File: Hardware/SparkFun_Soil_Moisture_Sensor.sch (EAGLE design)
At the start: 12 parts, among them Q1 2N3904

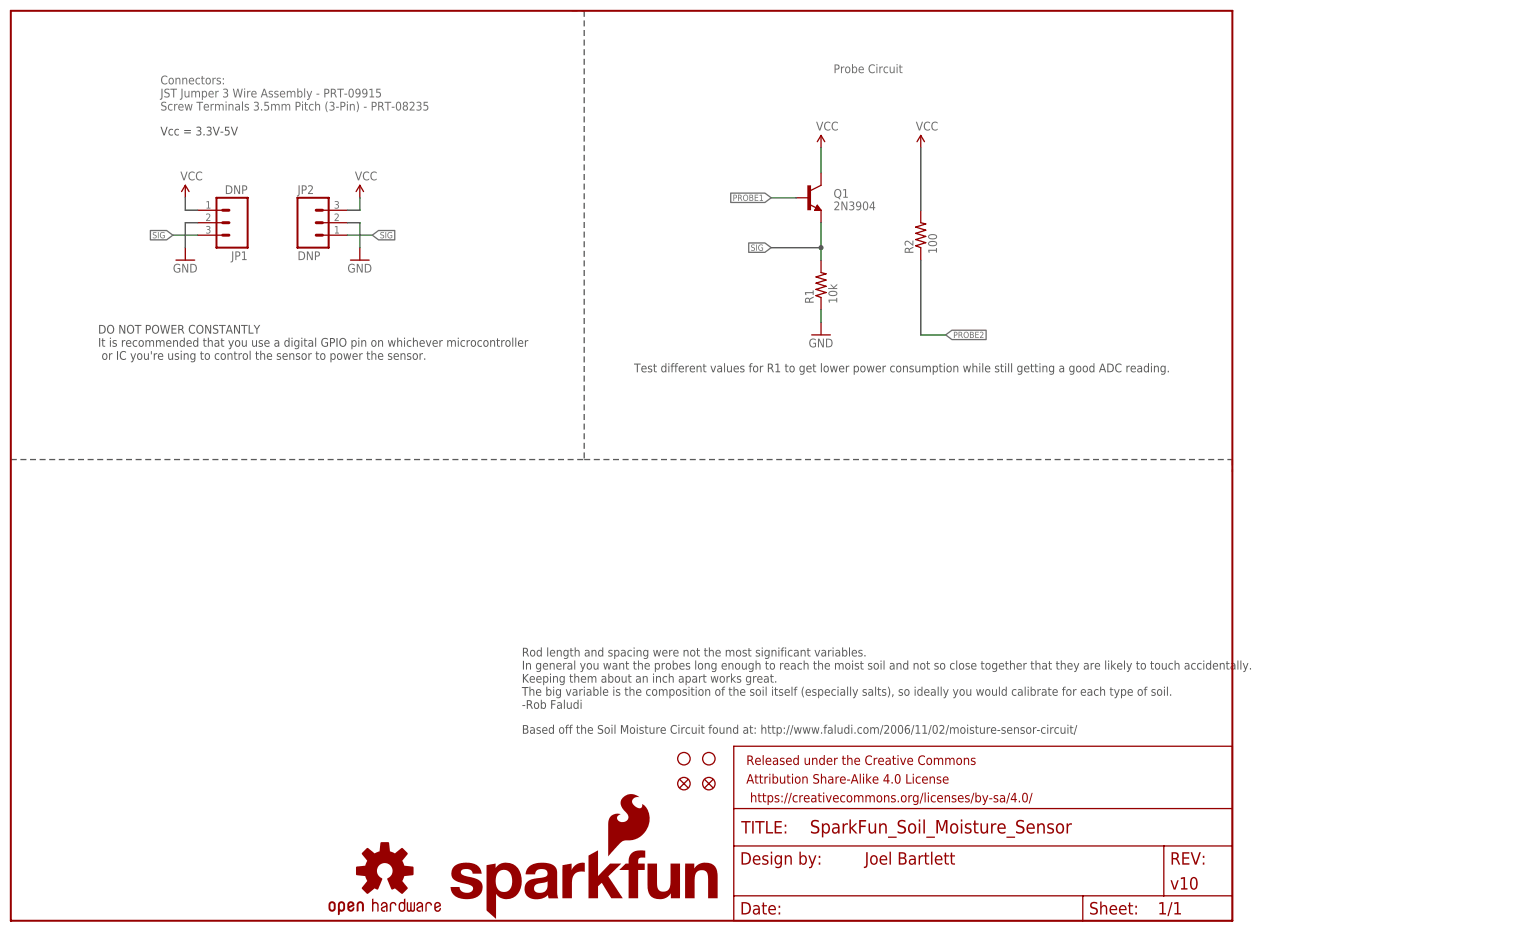
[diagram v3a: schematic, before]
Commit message: Added Locking 3-pin 3.5mm footprint
Added Locking 3-pin 3.5mm footprint for selective soldering.
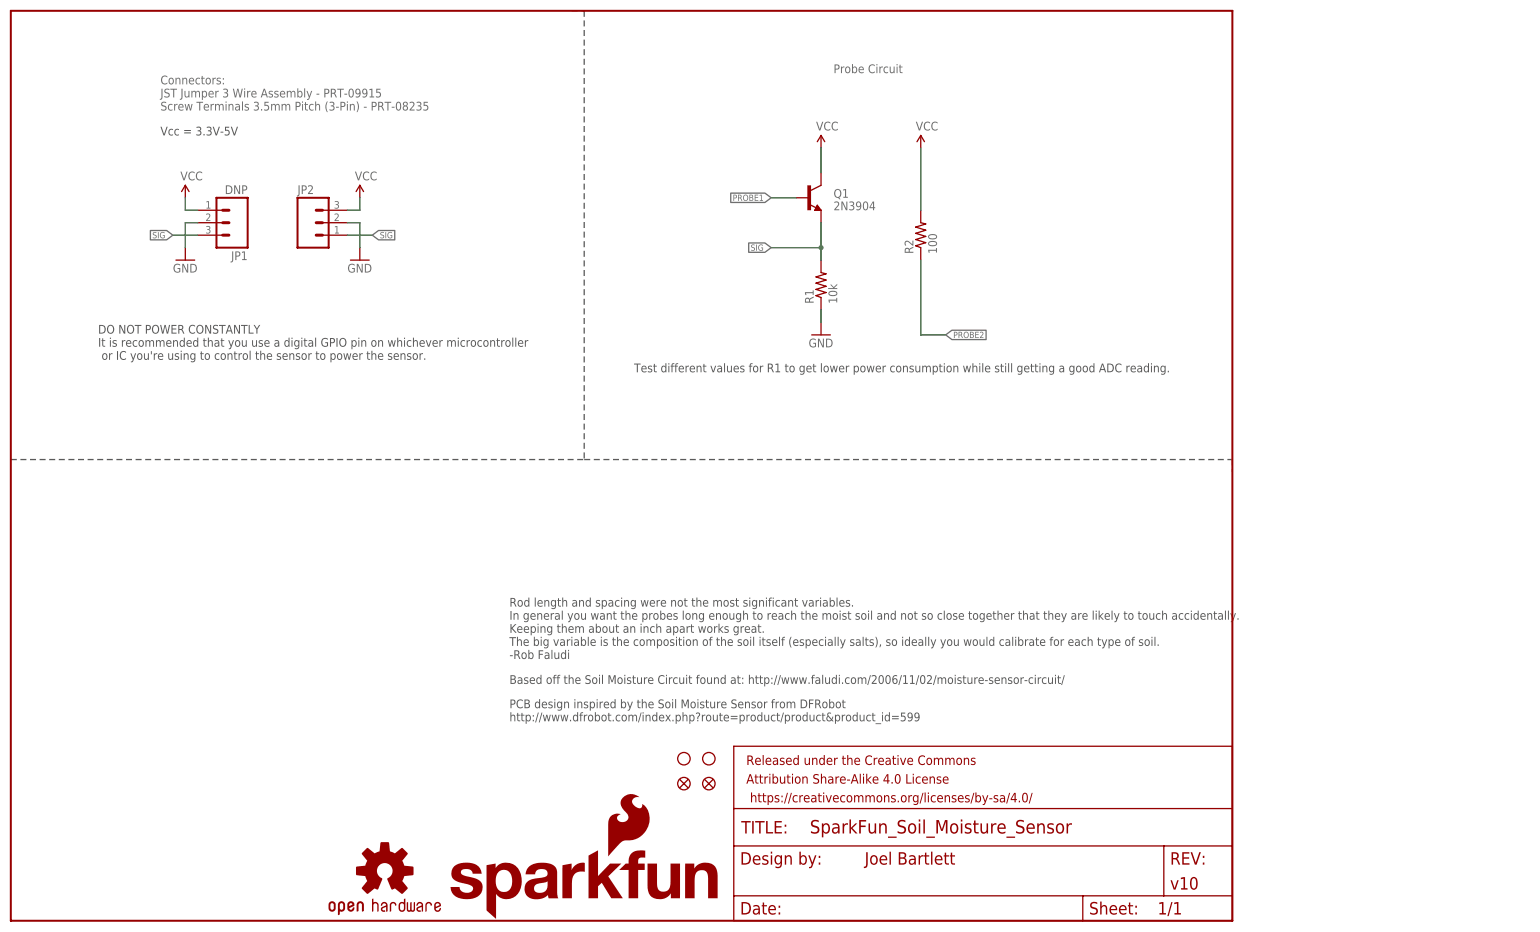
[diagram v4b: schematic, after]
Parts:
- JP2: value DNP -> (none); device SparkFun-Connectors:M03SCREW -> SparkFun-Connectors:M03SCREW_LOCK
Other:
- note added: "PCB design inspired by the Soil Moisture Sensor from DFRobot http://www.dfrobot.com/index.php?route=product/product&product_id=599"
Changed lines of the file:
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@@
 <part name="LOGO2" library="SparkFun-Aesthetics" deviceset="OSHW-LOGO" device="S"/>
 <part name="JP1" library="SparkFun-Connectors" deviceset="M03" device="POLAR" value="DNP"/>
-<part name="JP2" library="SparkFun-Connectors" deviceset="M03" device="SCREW" value="DNP"/>
 <part name="SUPPLY4" library="SparkFun-Aesthetics" deviceset="VCC" device=""/>
 <part name="GND3" library="SparkFun-Aesthetics" deviceset="GND" device=""/>
@@
 <part name="FID1" library="SparkFun-Aesthetics" deviceset="FIDUCIAL" device="1X2"/>
 <part name="FID2" library="SparkFun-Aesthetics" deviceset="FIDUCIAL" device="1X2"/>
+<part name="JP2" library="SparkFun-Connectors" deviceset="M03" device="SCREW_LOCK"/>
 </parts>
 <sheets>
@@
 <wire x1="114.3" y1="185.42" x2="116.84" y2="185.42" width="0.2032" layer="97" style="dashdot"/>
 <wire x1="116.84" y1="185.42" x2="116.84" y2="93.98" width="0.2032" layer="97" style="shortdash"/>
-<text x="104.14" y="38.1" size="1.778" layer="97">Based off the Soil Moisture Circuit found at: http://www.faludi.com/2006/11/02/moisture-sensor-circuit/</text>
-<text x="104.14" y="43.18" size="1.778" layer="97">Rod length and spacing were not the most significant variables.
+<text x="101.6" y="48.26" size="1.778" layer="97">Based off the Soil Moisture Circuit found at: http://www.faludi.com/2006/11/02/moisture-sensor-circuit/</text>
+<text x="101.6" y="53.34" size="1.778" layer="97">Rod length and spacing were not the most significant variables.
 In general you want the probes long enough to reach the moist soil and not so close together that they are likely to touch accidentally.
 Keeping them about an inch apart works great.
@@
 It is recommended that you use a digital GPIO pin on whichever microcontroller
  or IC you're using to control the sensor to power the sensor. </text>
+<text x="101.6" y="40.64" size="1.778" layer="97">PCB design inspired by the Soil Moisture Sensor from DFRobot
+http://www.dfrobot.com/index.php?route=product/product&amp;product_id=599</text>
 </plain>
 <instances>
@@
 <instance part="LOGO2" gate="G$1" x="76.2" y="10.16"/>
 <instance part="JP1" gate="G$1" x="45.72" y="142.24" rot="R180"/>
-<instance part="JP2" gate="G$1" x="60.96" y="142.24"/>
 <instance part="SUPPLY4" gate="G$1" x="35.56" y="147.32"/>
 <instance part="GND3" gate="1" x="35.56" y="134.62"/>
@@
 <instance part="FID1" gate="G$1" x="137.16" y="27.94"/>
 <instance part="FID2" gate="G$1" x="142.24" y="27.94"/>
+<instance part="JP2" gate="G$1" x="60.96" y="142.24"/>
 </instances>
 <busses>
@@
 </segment>
 <segment>
-<pinref part="JP2" gate="G$1" pin="1"/>
 <wire x1="68.58" y1="139.7" x2="73.66" y2="139.7" width="0.1524" layer="91"/>
 <label x="73.66" y="139.7" size="1.27" layer="95" xref="yes"/>
+<pinref part="JP2" gate="G$1" pin="1"/>
 </segment>
 </net>
